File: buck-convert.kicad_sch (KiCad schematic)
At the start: 11 parts, among them IC1 LMR36510FADDAR

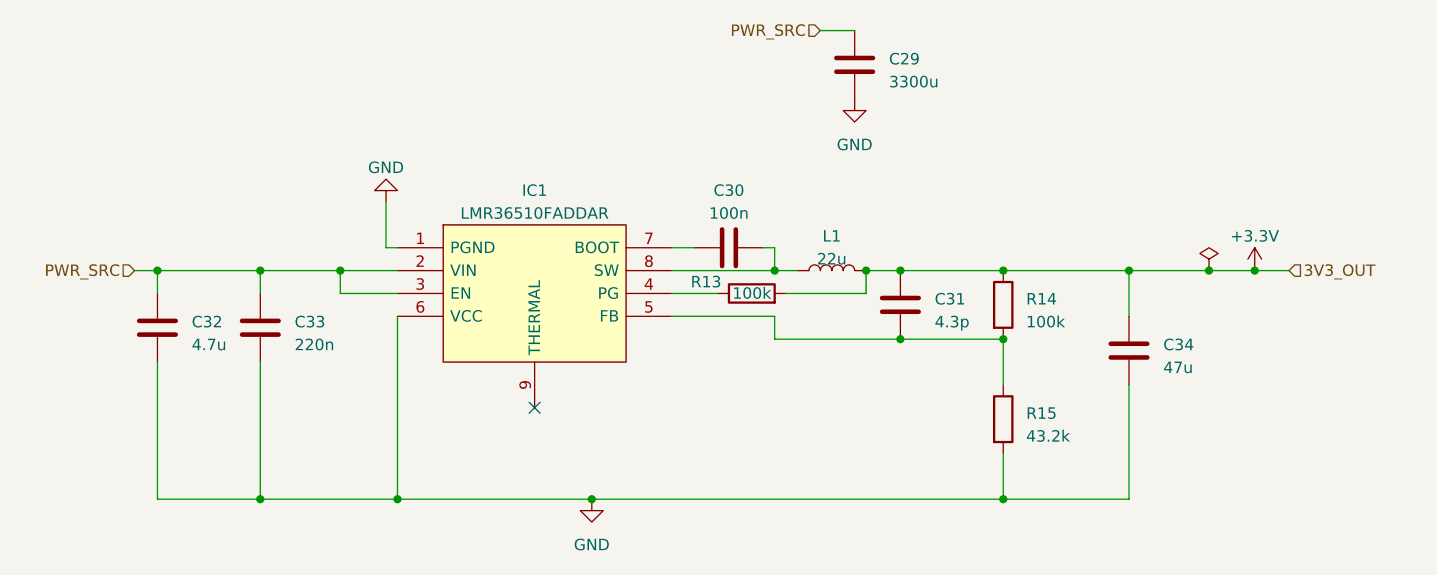
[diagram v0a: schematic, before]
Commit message: Add proper JST Connector
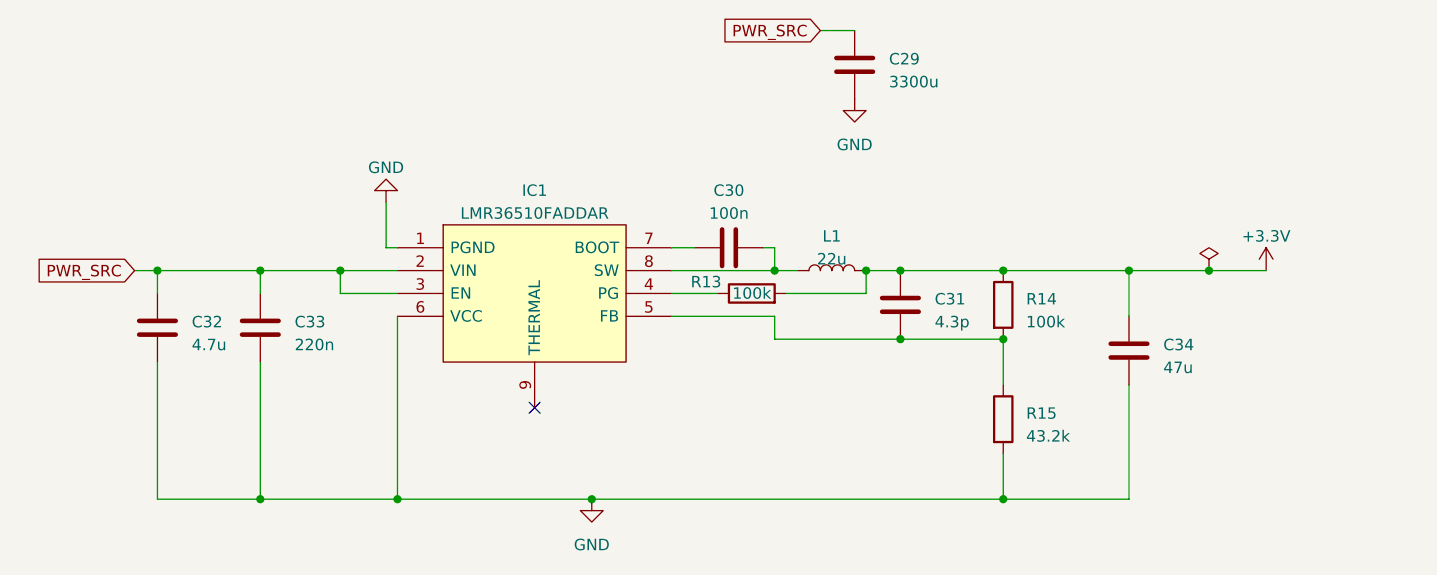
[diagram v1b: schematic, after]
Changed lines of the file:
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@@
   (junction (at 215.9 74.93) (diameter 0) (color 0 0 0 0)
-  )
-  (junction (at 229.87 74.93) (diameter 0) (color 0 0 0 0)
   )
   (no_connect (at 149.86 90.17))
@@
     (stroke (width 0) (type default))
   )
-  (wire (pts (xy 224.79 74.93) (xy 229.87 74.93))
+  (wire (pts (xy 224.79 74.93) (xy 231.14 74.93))
     (stroke (width 0) (type default))
   )
@@
     (stroke (width 0) (type default))
   )
-  (wire (pts (xy 229.87 74.93) (xy 233.68 74.93))
-    (stroke (width 0) (type default))
-  )
   (wire (pts (xy 107.95 100.33) (xy 119.38 100.33))
     (stroke (width 0) (type default))
@@
     (stroke (width 0) (type default))
   )
-  (hierarchical_label "PWR_SRC" (shape input) (at 105.41 74.93 180) (fields_autoplaced)
+  (global_label "PWR_SRC" (shape input) (at 105.41 74.93 180) (fields_autoplaced)
     (effects (font (size 1.27 1.27)) (justify right))
-  )
-  (hierarchical_label "3V3_OUT" (shape input) (at 233.68 74.93 0) (fields_autoplaced)
-    (effects (font (size 1.27 1.27)) (justify left))
-  )
-  (hierarchical_label "PWR_SRC" (shape input) (at 181.61 48.26 180) (fields_autoplaced)
+    (property "Intersheetrefs" "${INTERSHEET_REFS}" (at 93.7957 74.93 0)
+      (effects (font (size 1.27 1.27)) (justify right) hide)
+    )
+  )
+  (global_label "PWR_SRC" (shape input) (at 181.61 48.26 180) (fields_autoplaced)
     (effects (font (size 1.27 1.27)) (justify right))
+    (property "Intersheetrefs" "${INTERSHEET_REFS}" (at 169.9957 48.26 0)
+      (effects (font (size 1.27 1.27)) (justify right) hide)
+    )
   )
   (symbol (lib_id "Device:C") (at 119.38 81.28 0) (unit 1)
@@
     )
   )
-  (symbol (lib_id "power:+3.3V") (at 229.87 74.93 0) (unit 1)
+  (symbol (lib_id "power:+3.3V") (at 231.14 74.93 0) (unit 1)
     (in_bom yes) (on_board yes) (dnp no) (fields_autoplaced)
     (property "Reference" "#PWR048" (at 231.14 78.74 0)
       (effects (font (size 1.27 1.27)) hide)
     )
-    (property "Value" "+3.3V" (at 229.87 71.12 0)
-      (effects (font (size 1.27 1.27)))
-    )
-    (property "Footprint" "" (at 229.87 74.93 0)
-      (effects (font (size 1.27 1.27)) hide)
-    )
-    (property "Datasheet" "" (at 229.87 74.93 0)
-      (effects (font (size 1.27 1.27)) hide)
-    )
+    (property "Value" "+3.3V" (at 231.14 71.12 0)
+      (effects (font (size 1.27 1.27)))
+    )
+    (property "Footprint" "" (at 231.14 74.93 0)
+      (effects (font (size 1.27 1.27)) hide)
+    )
+    (property "Datasheet" "" (at 231.14 74.93 0)
+      (effects (font (size 1.27 1.27)) hide)
+    )

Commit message: fix ERC
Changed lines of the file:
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@@
     (stroke (width 0) (type default))
   )
-  (global_label "PWR_SRC" (shape input) (at 105.41 74.93 180) (fields_autoplaced)
+  (hierarchical_label "PWR_SRC" (shape input) (at 181.61 48.26 180) (fields_autoplaced)
     (effects (font (size 1.27 1.27)) (justify right))
-    (property "Intersheetrefs" "${INTERSHEET_REFS}" (at 93.7957 74.93 0)
-      (effects (font (size 1.27 1.27)) (justify right) hide)
-    )
   )
-  (global_label "PWR_SRC" (shape input) (at 181.61 48.26 180) (fields_autoplaced)
+  (hierarchical_label "PWR_SRC" (shape input) (at 105.41 74.93 180) (fields_autoplaced)
     (effects (font (size 1.27 1.27)) (justify right))
-    (property "Intersheetrefs" "${INTERSHEET_REFS}" (at 169.9957 48.26 0)
-      (effects (font (size 1.27 1.27)) (justify right) hide)
-    )
   )
   (symbol (lib_id "Device:C") (at 119.38 81.28 0) (unit 1)

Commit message: fixed ERC violations
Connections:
- net +3.3V renamed LMR_3v3
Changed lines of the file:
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@@
     (stroke (width 0) (type default))
+  )
+  (global_label "LMR_3v3" (shape input) (at 231.14 74.93 0) (fields_autoplaced)
+    (effects (font (size 1.27 1.27)) (justify left))
+    (property "Intersheetrefs" "${INTERSHEET_REFS}" (at 242.1495 74.93 0)
+      (effects (font (size 1.27 1.27)) (justify left) hide)
+    )
   )
   (hierarchical_label "PWR_SRC" (shape input) (at 181.61 48.26 180) (fields_autoplaced)
@@
         )
       )
-    )
-  )
-  (symbol (lib_id "power:+3.3V") (at 231.14 74.93 0) (unit 1)
-    (in_bom yes) (on_board yes) (dnp no) (fields_autoplaced)
-    (property "Reference" "#PWR048" (at 231.14 78.74 0)
-      (effects (font (size 1.27 1.27)) hide)
-    )
-    (property "Value" "+3.3V" (at 231.14 71.12 0)
-      (effects (font (size 1.27 1.27)))
-    )
-    (property "Footprint" "" (at 231.14 74.93 0)
-      (effects (font (size 1.27 1.27)) hide)
-    )
-    (property "Datasheet" "" (at 231.14 74.93 0)
-      (effects (font (size 1.27 1.27)) hide)
-    )
-    (pin "1")
-    (instances
-      (project "electrium-esc-v2"
-        (path "/be00c12c-11fa-42cb-8a0b-46fcd24b2ced/dedba472-5e9c-489a-b80e-963af35f7eb6"
-          (reference "#PWR048") (unit 1)
-        )
-      )

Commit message: Final schematic with no DRC errors
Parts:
- added J6: 3.3VJumper, Connector_PinHeader_2.54mm:PinHeader_1x02_P2.54mm_Vertical, symbol Connector:Conn_01x02_Pin
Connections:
- net LMR_3v3 renamed LMR_OUT
- net LMR_OUT: now also J6.2 (Pin_2)
- new net +3.3V: J6.1 (Pin_1)
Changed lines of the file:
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@@
+    (stroke (width 0) (type default))
+  )
+  (wire (pts (xy 233.68 74.93) (xy 236.22 74.93))
     (stroke (width 0) (type default))
   )
@@
     (stroke (width 0) (type default))
   )
-  (global_label "LMR_3v3" (shape input) (at 231.14 74.93 0) (fields_autoplaced)
-    (effects (font (size 1.27 1.27)) (justify left))
-    (property "Intersheetrefs" "${INTERSHEET_REFS}" (at 242.1495 74.93 0)
-      (effects (font (size 1.27 1.27)) (justify left) hide)
-    )
+  (label "LMR_OUT" (at 204.47 74.93 0) (fields_autoplaced)
+    (effects (font (size 1.27 1.27)) (justify left bottom))
   )
   (hierarchical_label "PWR_SRC" (shape input) (at 181.61 48.26 180) (fields_autoplaced)
@@
         (path "/be00c12c-11fa-42cb-8a0b-46fcd24b2ced/dedba472-5e9c-489a-b80e-963af35f7eb6"
           (reference "C33") (unit 1)
+        )
+      )
+    )
+  )
+  (symbol (lib_id "Connector:Conn_01x02_Pin") (at 233.68 69.85 270) (unit 1)
+    (in_bom yes) (on_board yes) (dnp no) (fields_autoplaced)
+    (property "Reference" "J6" (at 234.95 69.85 90)
+      (effects (font (size 1.27 1.27)) (justify left))
+    )
+    (property "Value" "3.3VJumper" (at 234.95 72.39 90)
+      (effects (font (size 1.27 1.27)) (justify left))
+    )
+    (property "Footprint" "Connector_PinHeader_2.54mm:PinHeader_1x02_P2.54mm_Vertical" (at 233.68 69.85 0)
+      (effects (font (size 1.27 1.27)) hide)
+    )
+    (property "Datasheet" "~" (at 233.68 69.85 0)
+      (effects (font (size 1.27 1.27)) hide)
+    )
+    (pin "1")
+    (pin "2")
+    (instances
+      (project "electrium-esc-v2"
+        (path "/be00c12c-11fa-42cb-8a0b-46fcd24b2ced/dedba472-5e9c-489a-b80e-963af35f7eb6"
+          (reference "J6") (unit 1)
         )
       )
@@
         )
       )
+    )
+  )
+  (symbol (lib_id "power:+3.3V") (at 236.22 74.93 180) (unit 1)
+    (in_bom yes) (on_board yes) (dnp no) (fields_autoplaced)
+    (property "Reference" "#PWR048" (at 236.22 71.12 0)
+      (effects (font (size 1.27 1.27)) hide)
+    )
+    (property "Value" "+3.3V" (at 236.22 80.01 0)
+      (effects (font (size 1.27 1.27)))
+    )
+    (property "Footprint" "" (at 236.22 74.93 0)
+      (effects (font (size 1.27 1.27)) hide)
+    )
+    (property "Datasheet" "" (at 236.22 74.93 0)
+      (effects (font (size 1.27 1.27)) hide)
+    )
+    (pin "1")
+    (instances
+      (project "electrium-esc-v2"
+        (path "/be00c12c-11fa-42cb-8a0b-46fcd24b2ced/dedba472-5e9c-489a-b80e-963af35f7eb6"
+          (reference "#PWR048") (unit 1)
+        )
+      )
